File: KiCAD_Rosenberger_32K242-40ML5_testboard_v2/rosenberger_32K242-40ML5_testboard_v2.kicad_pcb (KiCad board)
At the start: 6 copper layers, 58.6 x 38 mm, 2 parts, among them X1 SMA_Rosenberger_32K242-40ML5_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, X2 SMA_Rosenberger_32K242-40ML5_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

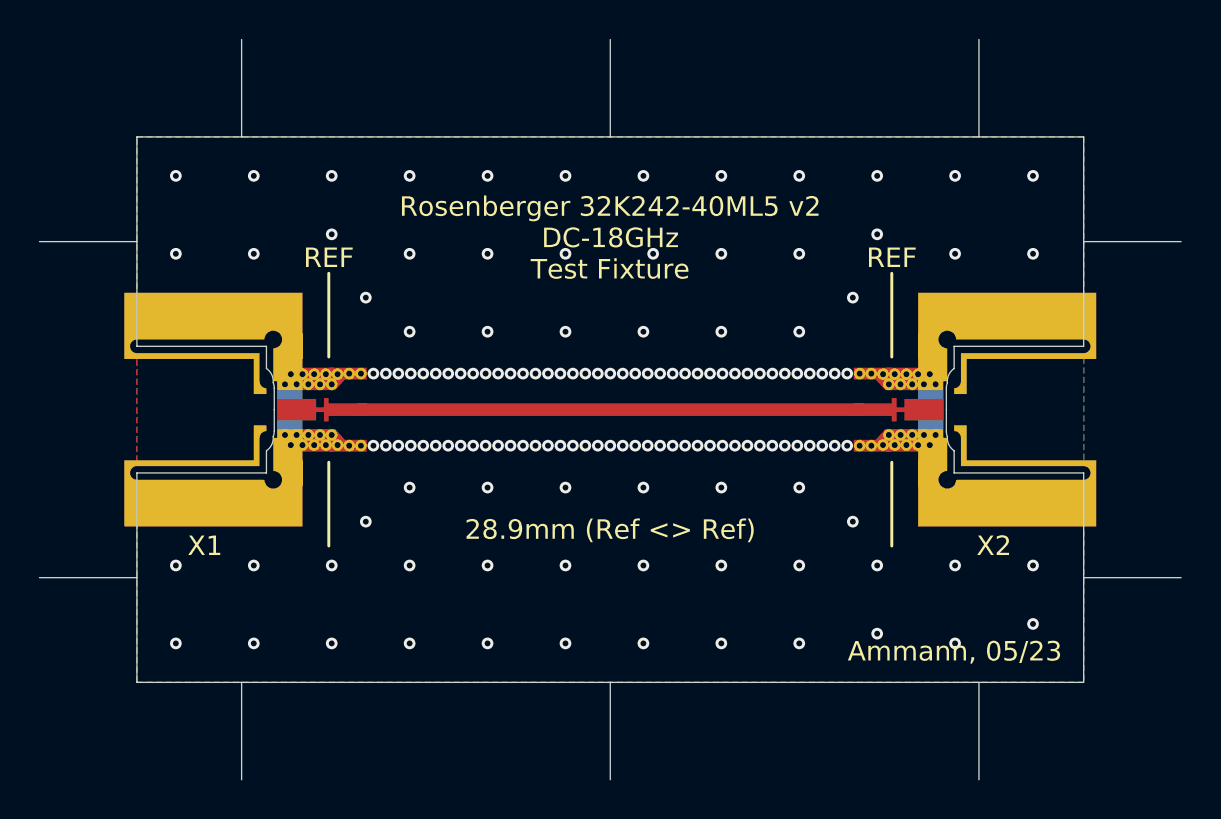
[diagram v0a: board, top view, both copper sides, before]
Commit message: add kicad footprint and pcb files after changing to Rosenberg STEP model - without filtering/cleaning up changed files! just sync.
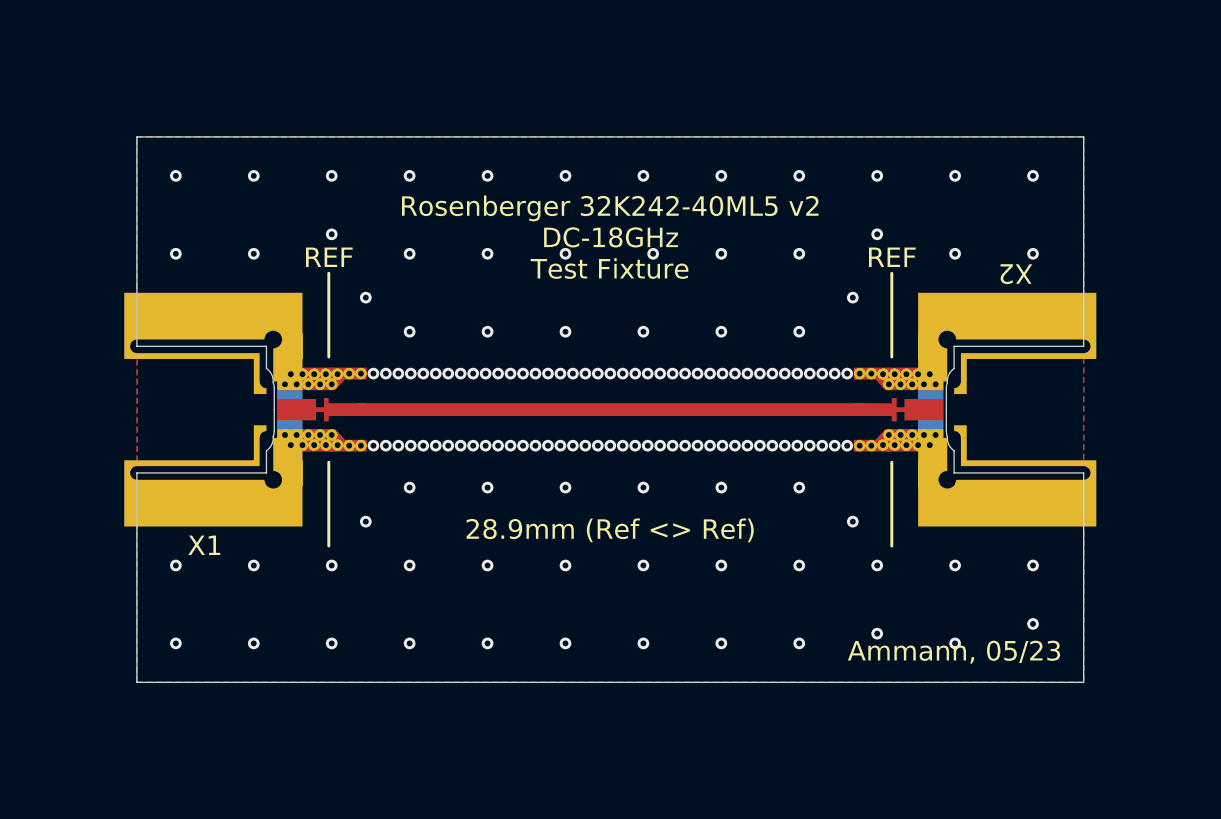
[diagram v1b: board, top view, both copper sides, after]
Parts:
- X1, X2: footprint AMMANN_RF_Connectors:Rosenberger_32K242-40ML5v2 -> RF_Connectors:Rosenberger_32K242-40ML5v2
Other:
- board size 58.6 x 38 mm -> 48.6 x 28 mm
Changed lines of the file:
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@@
   (net 1 "/RF_TRACE")
   (net 2 "GND")
-  (footprint "AMMANN_RF_Connectors:Rosenberger_32K242-40ML5v2" (layer "F.Cu")
+  (footprint "RF_Connectors:Rosenberger_32K242-40ML5v2" (layer "F.Cu")
     (at 0 14)
     (property "Manufacturer Part Number" "32K242-40ML5")
@@
       ))
     (pad "2" smd custom (at 6.65 0) (size 0.5 0.5) (layers "In3.Cu" "In4.Cu")
-      (net 2 "GND") (pinfunction "Ext") (pintype "passive") (thermal_bridge_angle 45)
+      (net 2 "GND") (pinfunction "Ext") (pintype "passive")
       (options (clearance outline) (anchor circle))
       (primitives
@@
       )
     )
-    (group "" (id 78fa9760-da8e-4bd4-b689-eae1f2f9e3c8)
+    (group "" (id 886a0fba-4fb5-40dd-a765-f8ac37a0425d)
       (members
-        0ea3bac1-8a3a-4a52-94aa-07d531f2c3eb
-        17a7113c-3034-4329-a173-3f0924e8c637
-        18354ae7-1072-4d7e-a521-3494b0104781
-        23dd42b7-a325-47b2-94ed-2af1d015892f
-        473527ce-d23b-4e72-8d68-d4a093c63799
-        6269d54a-ff1a-4604-99e3-f5317d8c58ce
-        6324c264-6f7d-49b1-8d06-e324dd797b94
-        7391f9e8-5f7d-465f-aa43-b00acb36242c
-        78b29fa4-b850-49ba-bef4-b94dc5510cd9
-        91e7b0f1-884a-49fc-8ac4-2c1a744501f5
-        accd4f64-e044-45b7-97d4-90a10035097a
-        c027481b-41a1-445d-ae24-79ddb5db8df9
-        c6894295-6e5a-4354-bb2e-7e36703ae697
-        cbe60467-0dc9-460c-8e7d-806f01ca5fb0
-        d52082e9-6a17-4764-8c1c-ee8ad93c1aee
-        e4c81170-ea9c-4ef9-b5bc-200b5182fec0
+        039aca1e-9136-48a8-9e6f-e119a92b4983
+        1a1868ca-7f10-45a1-aba2-c19a86f5c854
+        216757c1-ab6a-4b43-a7ad-ef89279ce8fc
+        2948e406-d042-48d1-b6e2-ba0b4d3139e2
+        31b3e819-d4f1-4acc-bca6-6cb16d27df00
+        593bfaeb-6a0e-4c20-81cd-c22e16e2922d
+        6f0f7a0c-b652-486d-a8ac-4ec47e28b06d
+        8df16860-adfb-4aea-afd7-867421cabee3
+        914caef2-ff7a-45bc-aaaf-f44957eff30a
+        95f2d7c8-444f-4a45-8ea8-ca23302c384e
+        9d961540-1b4c-4962-9bc5-d27de9ff483f
+        b6d6e82b-8cff-45a4-861d-952e35a0cf30
+        bc8602cc-e60c-4a06-a8fe-3488e278bd17
+        c2171692-20da-417c-ab0d-ca65392125f4
+        cd4ae547-f24a-4099-b2eb-f696ded4f8be
+        f2a05da5-7df1-4183-917d-743400a00b21
       )
     )
-    (model "./STP_60312202114307.stp"
+    (model "/home/oberstet/scm/oberstet/Multilayer_SMA2Microstrip/KiCAD_Rosenberger_32K242-40ML5_Footprint/RF_Connectors.pretty/32k242-40mxx_shrink.stp"
       (offset (xyz 7 0 0.47))
       (scale (xyz 1 1 1))
-      (rotate (xyz -90 0 90))
+      (rotate (xyz 90 90 90))
     )
   )
-  (footprint "AMMANN_RF_Connectors:Rosenberger_32K242-40ML5v2" (layer "F.Cu")
+  (footprint "RF_Connectors:Rosenberger_32K242-40ML5v2" (layer "F.Cu")
     (at 48.6 14 180)
     (property "Manufacturer Part Number" "32K242-40ML5")
@@
     (property "ki_keywords" "SMA coaxial connector Ammann 32K242-40ML5")
     (attr through_hole allow_soldermask_bridges)
-    (fp_text reference "X2" (at 4.6 -7 unlocked) (layer "F.SilkS")
+    (fp_text reference "X2" (at 3.5 7 180 unlocked) (layer "F.SilkS")
         (effects (font (size 1 1) (thickness 0.15)))
     )
@@
       ))
     (pad "2" smd custom (at 6.65 0 180) (size 0.5 0.5) (layers "In3.Cu" "In4.Cu")
-      (net 2 "GND") (pinfunction "Ext") (pintype "passive") (thermal_bridge_angle 45)
+      (net 2 "GND") (pinfunction "Ext") (pintype "passive")
       (options (clearance outline) (anchor circle))
       (primitives
@@
       )
     )
-    (group "" (id d9e3abeb-fb71-4deb-a388-a303dd9c4b15)
+    (group "" (id 17f8a721-ccbe-41b4-99c3-88367c128404)
       (members
-        123c6191-1950-4db8-954c-402b0e92b9ca
-        1355294a-49d2-4f48-8392-e0aa615ac5c8
-        153947bf-9357-42ff-a1a2-87d40f45cc67
-        21841daf-a353-42ea-b189-f5c1ad087ef7
-        3832878e-79d6-494f-a830-579f3999fcbe
-        56c26148-7155-4cf6-ac8d-95dbb0919d20
-        840bacb9-e1f4-4345-ab34-7d4f4f6254ad
-        857b430c-19f7-4124-8287-e0f442ea0f16
-        92ddf2c5-02b9-44b8-b2d4-1d57604c8470
-        965e5181-6fc9-486a-8fd2-dce874b78bb8
-        aea9c51f-9385-4c6c-961f-ed55a7c74b1a
-        b958f3ae-8150-4bbe-9909-42725cceb6c1
-        c032d075-3dbe-444f-a1da-8c8b8dba426e
-        c76a5ac9-b05e-40ce-bda1-57300b9ea26d
-        f6cb906b-dbc1-434e-8119-e49611e601a4
-        f7bc8824-f451-448c-b568-97553f9d446c
+        00244706-05fd-4c51-935b-800066885f96
+        073e9cd9-0770-4fb1-bce9-f193f3216c4a
+        10281f72-bd8f-4ee1-bfb9-817b3a9de0f1
+        1997523d-248d-4ae8-a79c-06f3b3e48e88
+        24c92bff-5987-4006-9d44-1165607ab271
+        40e3e6d5-e85e-45e7-ac67-420ab0ec6dd9
+        617c32b0-12df-44d2-8abd-38aac958c5b8
+        80c8e159-c5e9-4045-8603-afe6be4ff440
+        84c578e3-d4b4-4cf1-ab70-532434bf3c4e
+        99602bc1-dd16-4eff-a4f9-766a9462c0ef
+        ac01a7a1-80c0-48d5-8a0b-4fe46423deae
+        b4cc7752-7fb5-4052-9eed-2b132722a98c
+        cdfa8ccb-99bd-467e-822e-0d96122feeeb
+        ea93ff04-04ab-4bc4-8d13-c99b4d07152b
+        f61f3ed6-84d0-4781-8b08-f9d0d7ba3b12
+        feef09a8-27a0-4471-b372-a92dc79ab620
       )
     )
-    (model "./STP_60312202114307.stp"
+    (model "/home/oberstet/scm/oberstet/Multilayer_SMA2Microstrip/KiCAD_Rosenberger_32K242-40ML5_Footprint/RF_Connectors.pretty/32k242-40mxx_shrink.stp"
       (offset (xyz 7 0 0.47))
       (scale (xyz 1 1 1))
-      (rotate (xyz -90 0 90))
+      (rotate (xyz 90 90 90))
     )
   )
@@
   (gr_circle (center 43.225 28.8) (end 43.225 28)
     (stroke (width 0.05) (type default)) (fill none) (layer "Dwgs.User"))
-  (gr_line (start -5 22.625) (end 0 22.625)
-    (stroke (width 0.05588) (type default)) (layer "Edge.Cuts"))
   (gr_line (start 48.6 17.25) (end 48.6 28)
     (stroke (width 0.05) (type default)) (layer "Edge.Cuts"))
-  (gr_line (start 48.6 5.375) (end 53.6 5.375)
-    (stroke (width 0.05588) (type default)) (layer "Edge.Cuts"))
-  (gr_line (start 5.375 28) (end 5.375 33)
-    (stroke (width 0.05588) (type default)) (layer "Edge.Cuts"))
-  (gr_line (start 48.6 22.625) (end 53.6 22.625)
-    (stroke (width 0.05588) (type default)) (layer "Edge.Cuts"))
-  (gr_line (start 43.225 0) (end 43.225 -5)
-    (stroke (width 0.05588) (type default)) (layer "Edge.Cuts"))
-  (gr_line (start -5 5.375) (end 0 5.375)
-    (stroke (width 0.05588) (type default)) (layer "Edge.Cuts"))
   (gr_line (start 48.6 0) (end 48.6 10.75)
     (stroke (width 0.05) (type default)) (layer "Edge.Cuts"))
   (gr_line (start 0 0) (end 48.6 0)
     (stroke (width 0.05) (type default)) (layer "Edge.Cuts"))
-  (gr_line (start 43.225 28) (end 43.225 33)
-    (stroke (width 0.05588) (type default)) (layer "Edge.Cuts"))
-  (gr_line (start 5.375 0) (end 5.375 -5)
-    (stroke (width 0.05588) (type default)) (layer "Edge.Cuts"))
-  (gr_line (start 24.3 0) (end 24.3 -5)
-    (stroke (width 0.05588) (type default)) (layer "Edge.Cuts"))
   (gr_line (start 0 28) (end 0 17.25)
     (stroke (width 0.05) (type default)) (layer "Edge.Cuts"))
   (gr_line (start 48.6 28) (end 0 28)
     (stroke (width 0.05) (type default)) (layer "Edge.Cuts"))
-  (gr_line (start 24.3 28) (end 24.3 33)
-    (stroke (width 0.05588) (type default)) (layer "Edge.Cuts"))
   (gr_line (start 0 10.75) (end 0 0)
     (stroke (width 0.05) (type default)) (layer "Edge.Cuts"))
